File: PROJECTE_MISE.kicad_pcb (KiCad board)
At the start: 2 copper layers, 75 x 80 mm, 46 parts, among them IC1 MSP430FR2355TPT, J1 conn_DFrobot, J10 SDA_{TP}, J11 SCL_{TP}, J12 SCL_{TP-GND}, J13 SPI_{TP-MISO}, J14 SPI_{TP-SS}, J15 SPI_{TP-SCLK}, J16 SPI_{TP-MOSI}, J17 SPI_{TP-GND}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

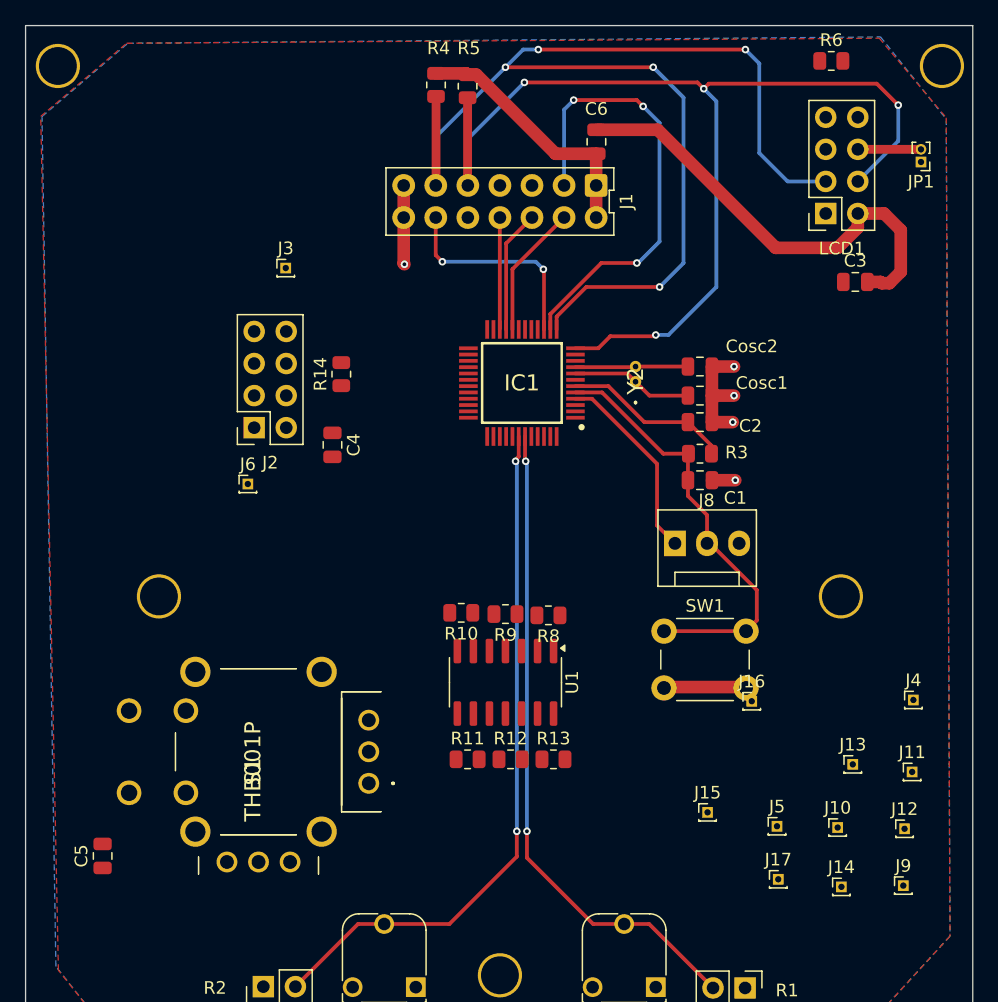
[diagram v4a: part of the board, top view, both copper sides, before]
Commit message: layout ESP module and comparators
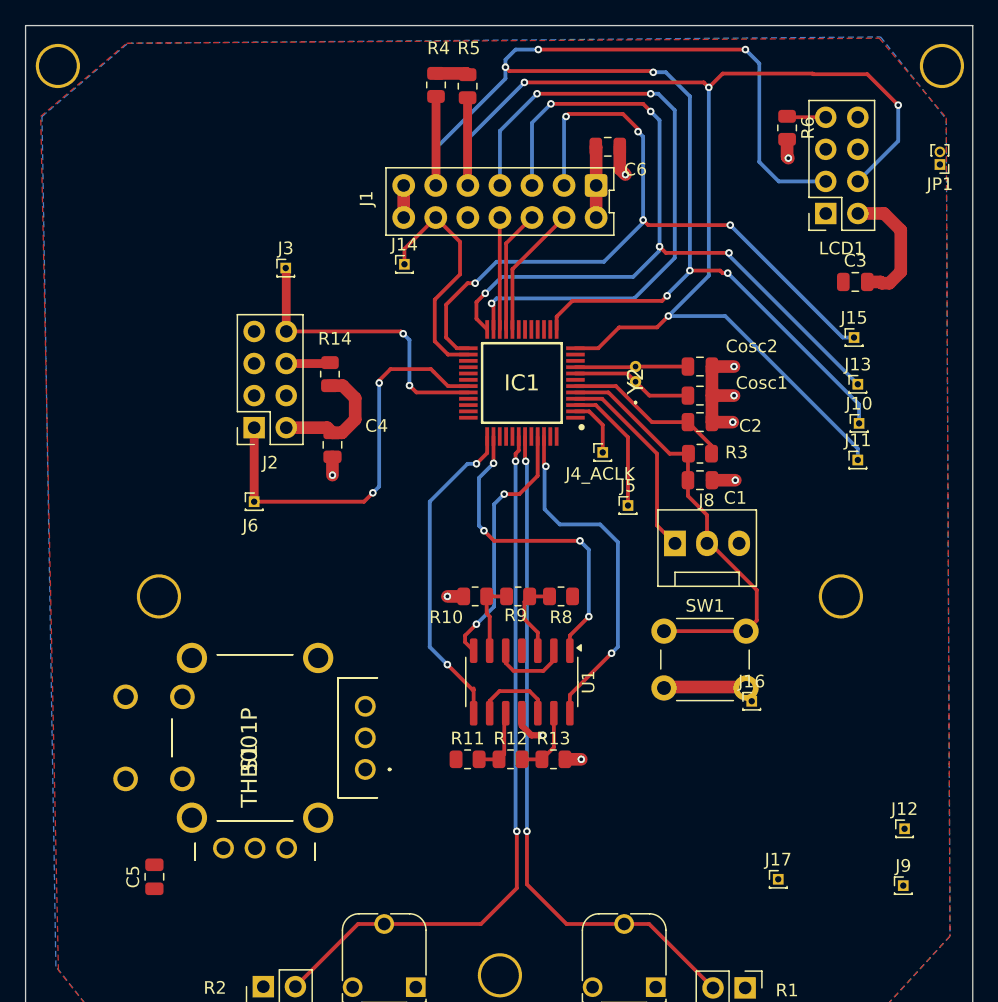
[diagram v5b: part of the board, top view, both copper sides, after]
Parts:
- J4_ACLK: renamed from J4; value conn_ACLK_{TP} -> ACLK_{TP}
- moved J14 60.2 mm to (99.0, 78.4)
- moved J15 39.3 mm to (134.6, 84.2)
- moved J10 32.0 mm to (135.0, 91.0)
- moved J4_ACLK 31.5 mm to (114.7, 93.3)
- moved J13 30.1 mm to (134.9, 87.9)
- moved J5 28.0 mm to (116.7, 97.5)
- moved J11 25.1 mm to (134.9, 93.9)
- moved R6 6.35 mm to (129.3, 67.6), turned to -90 degrees
- moved C5 4.42 mm to (79.2, 126.9)
- moved R8 1.80 mm to (111.4, 104.7)
- moved R9 1.72 mm to (108.0, 104.7)
- moved R10 1.70 mm to (104.6, 104.7)
- moved JP1 1.51 mm to (141.4, 70.5)
- moved J6 1.49 mm to (87.1, 97.2)
- moved U1 1.29 mm to (108.3, 111.5)
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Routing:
- net /SPI_MISO: track 0.00 -> 65.6 mm, vias 0 -> 5
- net /SPI_MOSI: track 0.00 -> 49.7 mm, vias 0 -> 3
- net /RX_{ESP}: track 0.00 -> 32.7 mm, vias 0 -> 2
- net /JTK_{L}: track 0.00 -> 27.9 mm, vias 0 -> 2
- net /SPI_SCLK: track 36.3 -> 62.9 mm, vias 3 -> 5
- net /JTK_{R}: track 0.00 -> 25.8 mm, vias 0 -> 2
- net /JTK_{F}: track 0.00 -> 25.7 mm, vias 0 -> 4
- net /TX_{ESP}: track 0.00 -> 23.6 mm, vias 0 -> 2
- net /I2C_SDA: track 94.1 -> 115.7 mm, vias 5 -> 7
- net /JTK_{B}: track 0.00 -> 20.3 mm, vias 0 -> 2
- net /I2C_SCL: track 84.3 -> 103.7 mm
- net GND: track 60.9 -> 41.7 mm, vias 5 -> 10
- net /SMCLK_{TP}: track 0.00 -> 10.6 mm
- net /TH_{F}: track 0.00 -> 6.48 mm
- net /AO1: track 0.00 -> 6.47 mm
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
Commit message: layout new placement and nee changes
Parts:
- J10, J11, J12, J13, J14, J15, J16, J17, J3, J5, J6, J9: footprint Connector_PinHeader_1.00mm:PinHeader_1x01_P1.00mm_Vertical -> Connector_PinHeader_1.27mm:PinHeader_1x01_P1.27mm_Vertical
- J4: renamed from J4_ACLK; value ACLK_{TP} -> conn_ACLK_{TP}; footprint Connector_PinHeader_1.00mm:PinHeader_1x01_P1.00mm_Vertical -> Connector_PinHeader_1.27mm:PinHeader_1x01_P1.27mm_Vertical
- JP1: footprint Connector_PinHeader_1.00mm:PinHeader_1x02_P1.00mm_Vertical -> Connector_PinHeader_1.27mm:PinHeader_2x01_P1.27mm_Vertical
- LCD1: footprint Connector_PinSocket_2.54mm:PinSocket_2x04_P2.54mm_Vertical -> MiSE:LCD_2x16_I2C(Midas)
- moved J3 77.8 mm to (158.2, 115.3)
- moved J14 75.4 mm to (157.7, 125.8)
- moved J6 74.8 mm to (158.3, 120.0)
- moved R6 64.4 mm to (71.6, 96.1), turned to 180 degrees
- moved C3 47.9 mm to (134.3, 127.7)
- moved C6 44.7 mm to (80.0, 96.9)
- moved J16 40.9 mm to (167.4, 112.8)
- moved J17 38.3 mm to (166.8, 130.1)
- moved J10 34.2 mm to (167.0, 103.0)
- moved J11 34.2 mm to (166.9, 105.9)
- moved J13 34.2 mm to (166.9, 99.9)
- moved J15 34.2 mm to (166.6, 96.2)
- moved R4 30.8 mm to (126.1, 82.7)
- moved JP1 29.5 mm to (140.5, 100.0), turned to 90 degrees
- moved J12 28.9 mm to (167.2, 119.1)
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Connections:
- IC1 pad 14: unconnected-(IC1-P4.5/UCB1CLK-Pad14) -> /~{RST_{LCD}}
- J2 pad 1: /RX_{ESP} -> GND
- J2 pad 2: +3V3 -> /TX_{ESP}
- J2 pad 4: unconnected-(J2-Pin_4-Pad4) -> /~{EN_{ESP}}
- J2 pad 6: /~{EN_{ESP}} -> unconnected-(J2-Pin_6-Pad6)
- J2 pad 7: GND -> /RX_{ESP}
- J2 pad 8: /TX_{ESP} -> +3V3
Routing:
- net /I2C_SDA: track 115.7 -> 0.00 mm, vias 7 -> 0
- net /I2C_SCL: track 103.7 -> 0.00 mm, vias 4 -> 0
- net /SPI_MISO: track 65.6 -> 0.00 mm, vias 5 -> 0
- net /SPI_SCLK: track 62.9 -> 0.00 mm, vias 5 -> 0
- net /LDR_{R}: track 56.7 -> 0.00 mm, vias 2 -> 0
- net /LDR_{L}: track 53.7 -> 0.00 mm, vias 2 -> 0
- net /SPI_MOSI: track 49.7 -> 0.00 mm, vias 3 -> 0
- net GND: track 41.7 -> 0.00 mm, vias 10 -> 0
- net /SBW_{TDIO}: track 34.3 -> 0.00 mm
- net /RX_{ESP}: track 32.7 -> 0.00 mm, vias 2 -> 0
- net +3V3: track 31.7 -> 0.00 mm
- net /JTK_{L}: track 27.9 -> 0.00 mm, vias 2 -> 0
- net /JTK_{R}: track 25.8 -> 0.00 mm, vias 2 -> 0
- net /JTK_{F}: track 25.7 -> 0.00 mm, vias 4 -> 0
- net /TX_{ESP}: track 23.6 -> 0.00 mm, vias 2 -> 0
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- removed copper zone on F.Cu, net +3V3
- removed copper zone on B.Cu, net GND

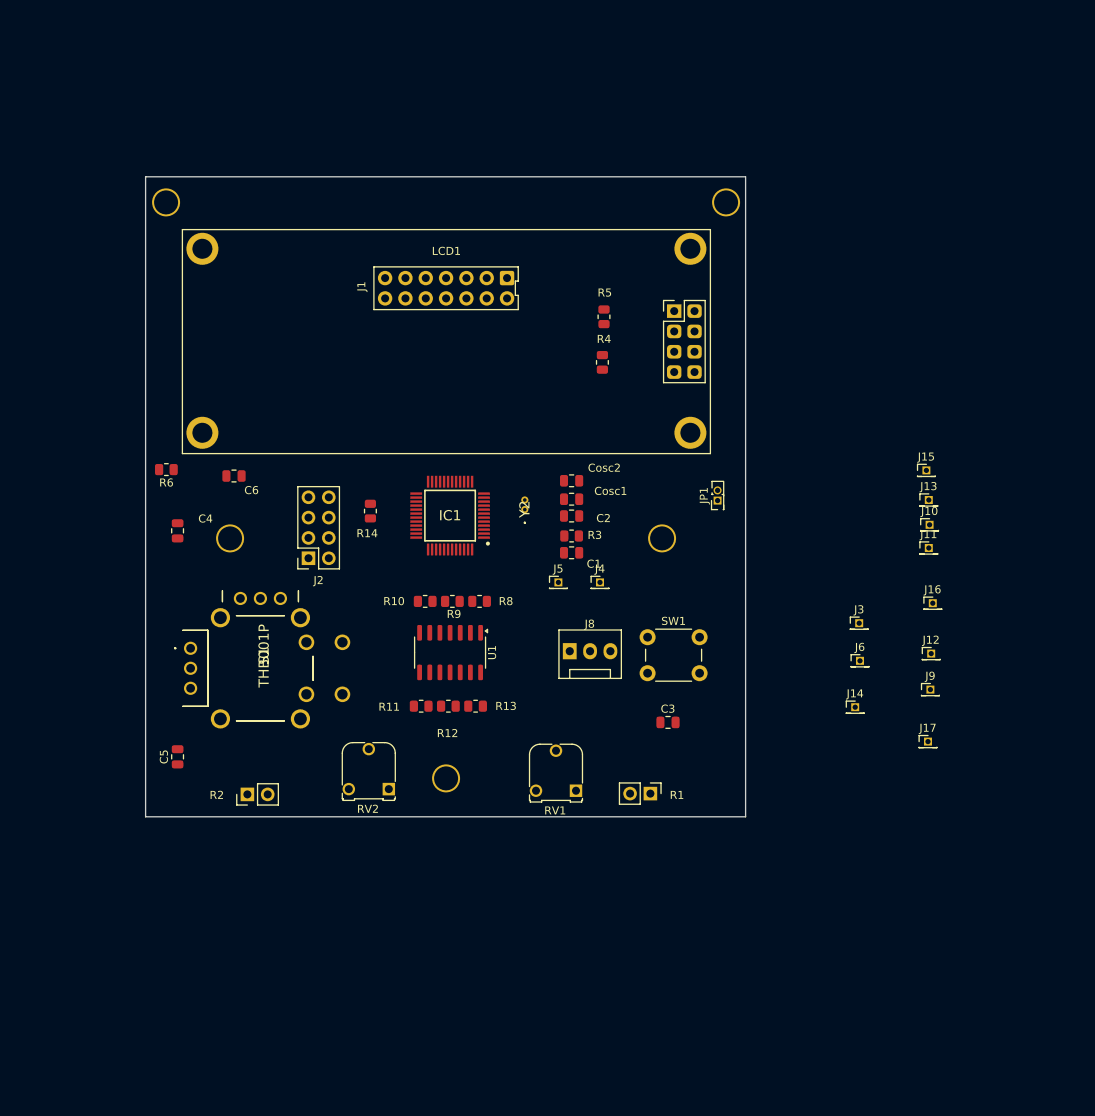
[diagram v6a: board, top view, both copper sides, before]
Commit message: update layout - routing
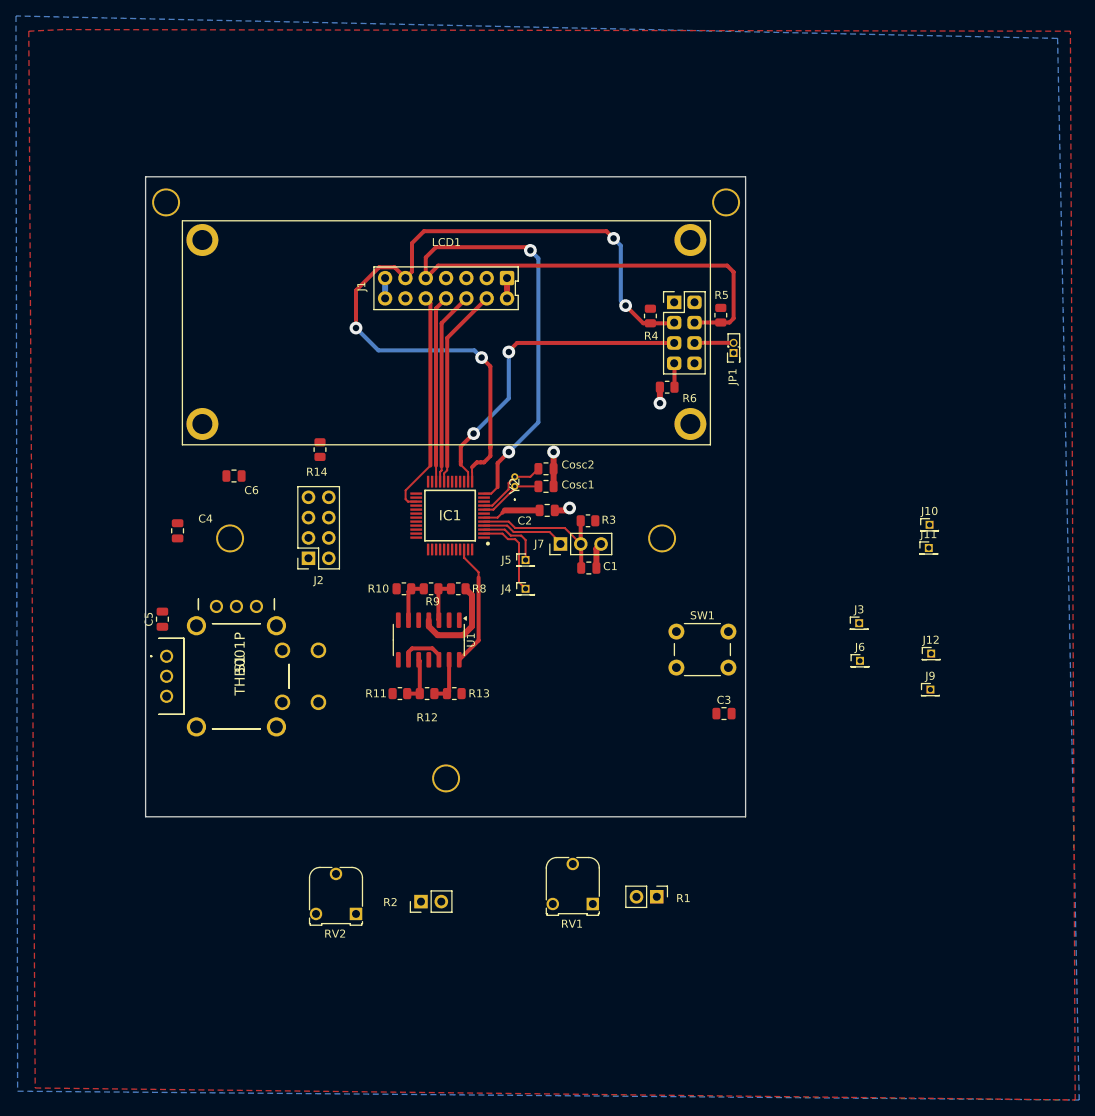
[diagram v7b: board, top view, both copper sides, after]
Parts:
- removed J13: SPI_{TP-MISO}, Connector_PinHeader_1.27mm:PinHeader_1x01_P1.27mm_Vertical
- removed J14: SPI_{TP-SS}, Connector_PinHeader_1.27mm:PinHeader_1x01_P1.27mm_Vertical
- removed J15: SPI_{TP-SCLK}, Connector_PinHeader_1.27mm:PinHeader_1x01_P1.27mm_Vertical
- removed J16: SPI_{TP-MOSI}, Connector_PinHeader_1.27mm:PinHeader_1x01_P1.27mm_Vertical
- removed J17: SPI_{TP-GND}, Connector_PinHeader_1.27mm:PinHeader_1x01_P1.27mm_Vertical
- removed J8: conn_SBW, Connector:FanPinHeader_1x03_P2.54mm_Vertical
- added J7: conn_SBW, Connector_PinHeader_2.54mm:PinHeader_1x03_P2.54mm_Vertical, F.Cu at (120.9, 105.4)
- moved R6 63.4 mm to (134.2, 85.8)
- moved R2 25.5 mm to (103.4, 150.1)
- moved JP1 18.6 mm to (142.5, 81.5)
- moved C5 17.3 mm to (71.1, 114.8)
- moved RV2 16.1 mm to (95.3, 151.6)
- moved R5 14.6 mm to (140.9, 76.8)
- moved RV1 14.3 mm to (124.9, 150.4)
- moved R1 12.9 mm to (132.9, 149.5)
- moved R14 9.94 mm to (90.8, 93.6)
- moved J4 9.33 mm to (116.5, 111.0)
- moved R4 8.35 mm to (132.1, 76.9)
- moved C3 7.09 mm to (141.3, 126.6)
- moved J5 4.96 mm to (116.5, 107.4)
- moved SW1 3.67 mm to (135.3, 116.3)
- moved Cosc1 3.58 mm to (119.0, 98.2)
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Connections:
- IC1 pad 23: /SPI_MOSI -> unconnected-(IC1-P4.3/UCA1TXD/UCA1SIMO/~{UCA1TXD}-Pad23)
- IC1 pad 24: /SPI_MISO -> unconnected-(IC1-P4.2/UCA1RXD/UCA1SOMI/~{UCA1RXD}-Pad24)
- IC1 pad 25: /SPI_SCLK -> unconnected-(IC1-P4.1/UCA1CLK-Pad25)
- IC1 pad 26: /SPI_SS -> unconnected-(IC1-P4.0/UCA1STE/ISOTXD/ISORXD-Pad26)
- J1 pad 12: /SPI_SS -> unconnected-(J1-Pin_12-Pad12)
- J1 pad 3: /SPI_SCLK -> unconnected-(J1-Pin_3-Pad3)
- J1 pad 5: /SPI_MISO -> unconnected-(J1-Pin_5-Pad5)
- J1 pad 7: /SPI_MOSI -> unconnected-(J1-Pin_7-Pad7)
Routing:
- net /I2C_SCL: track 0.00 -> 100.9 mm, vias 0 -> 2
- net /I2C_SDA: track 0.00 -> 94.6 mm, vias 0 -> 4
- net /~{RST_{LCD}}: track 0.00 -> 40.3 mm, vias 0 -> 2
- net /P8: track 0.00 -> 28.1 mm
- net /P0: track 0.00 -> 25.1 mm
- net /P1: track 0.00 -> 24.3 mm
- net /P2: track 0.00 -> 23.6 mm
- net +3V3: track 0.00 -> 22.0 mm
- net /SBW_{TDIO}: track 0.00 -> 19.2 mm
- net /JTK_{L}: track 0.00 -> 15.5 mm
- net GND: track 0.00 -> 14.1 mm, vias 0 -> 3
- net /SBW_{TCK}: track 0.00 -> 11.1 mm
- net /ACLK_{TP}: track 0.00 -> 10.9 mm
- net /XT1OUT: track 0.00 -> 9.17 mm
- net /SMCLK_{TP}: track 0.00 -> 8.24 mm
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- added copper zone on F.Cu, net +3V3
- added copper zone on B.Cu, net GND

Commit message: layout finished but it has to be checked
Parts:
- removed J10: SDA_{TP}, Connector_PinHeader_1.27mm:PinHeader_1x01_P1.27mm_Vertical
- removed J11: SCL_{TP}, Connector_PinHeader_1.27mm:PinHeader_1x01_P1.27mm_Vertical
- removed J12: SCL_{TP-GND}, Connector_PinHeader_1.27mm:PinHeader_1x01_P1.27mm_Vertical
- removed J9: SDA_{TP-GND}, Connector_PinHeader_1.27mm:PinHeader_1x01_P1.27mm_Vertical
- moved J6 87.6 mm to (72.4, 102.8)
- moved J3 86.1 mm to (72.5, 106.8)
- moved C3 59.3 mm to (131.9, 68.1), turned to 90 degrees
- moved C6 43.0 mm to (113.2, 69.5), turned to 180 degrees
- moved R2 24.0 mm to (84.5, 135.3)
- moved S1 21.5 mm to (93.1, 120.2), turned to -90 degrees
- moved SW1 20.8 mm to (132.9, 95.7)
- moved RV2 17.3 mm to (99.7, 134.9)
- moved RV1 16.4 mm to (121.0, 134.4)
- moved C4 16.0 mm to (85.1, 93.3)
- moved R1 16.0 mm to (129.5, 133.9)
- moved J2 14.9 mm to (77.1, 98.8)
- moved R8 13.9 mm to (116.3, 122.2)
- moved R10 13.3 mm to (113.8, 115.5), turned to 90 degrees
- moved R9 12.1 mm to (113.8, 118.9), turned to 90 degrees
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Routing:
- net GND: track 14.1 -> 65.3 mm, vias 3 -> 6
- net /RX_{ESP}: track 0.00 -> 47.3 mm
- net /JTK_{SEL}: track 0.00 -> 45.9 mm, vias 0 -> 2
- net /LDR_{R}: track 0.00 -> 43.0 mm
- net /AO2: track 0.00 -> 42.9 mm, vias 0 -> 2
- net /LDR_{L}: track 0.00 -> 42.9 mm
- net /JTK_{F}: track 0.00 -> 41.8 mm, vias 0 -> 2
- net /TX_{ESP}: track 0.00 -> 35.7 mm
- net +3V3: track 22.0 -> 55.2 mm, vias 0 -> 2
- net /AO1: track 5.92 -> 25.3 mm
- net /SBW_{TDIO}: track 19.2 -> 38.0 mm
- net /JTK_{B}: track 0.00 -> 11.4 mm
- net /JTK_{L}: track 15.5 -> 26.5 mm, vias 0 -> 2
- net /JTK_{R}: track 0.00 -> 10.4 mm
- net /I2C_SCL: track 100.9 -> 109.9 mm
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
